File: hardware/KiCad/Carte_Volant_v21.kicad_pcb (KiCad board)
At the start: 4 copper layers, 71.1 x 78.7 mm, 53 parts, among them J1 RJ45_CANBUS_copy, J2 Conn_01x03, J3 Conn_01x40, J7 Conn_01x03, Q2 FDN337N, U1 TSR_1-2450, U2 STM32H103-OlimexBoard, U3 MCP2561-E-SN

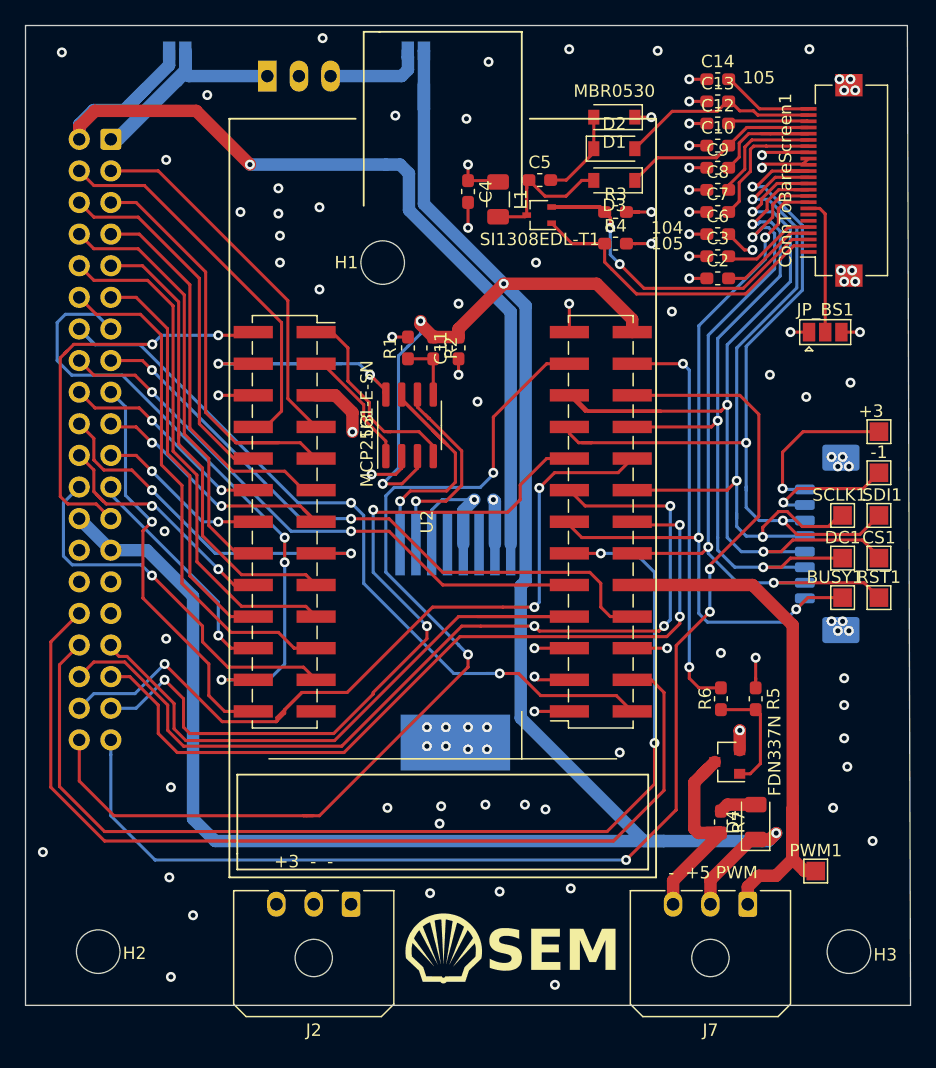
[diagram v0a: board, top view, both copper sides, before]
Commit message: errata correction : RJ45 connector + common volatge source + added 3d models + logo + ...
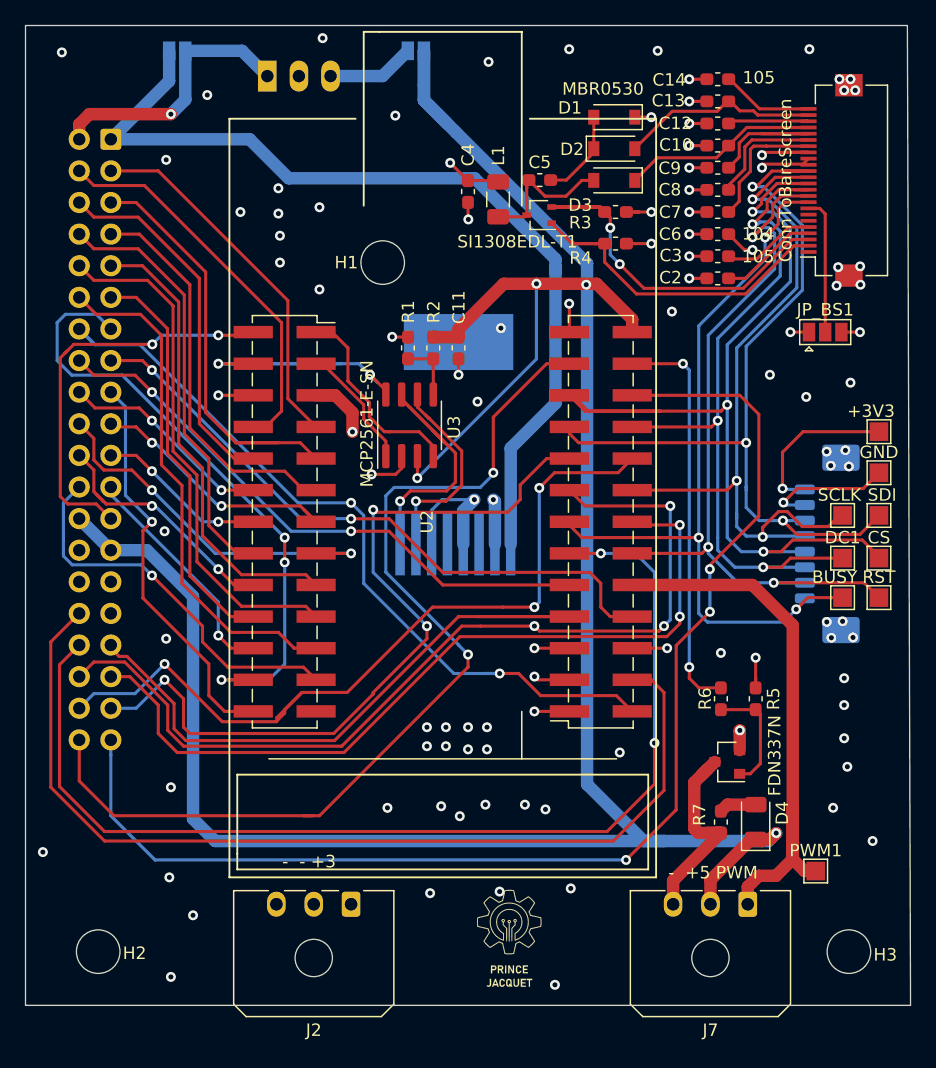
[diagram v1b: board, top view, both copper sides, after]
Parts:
- removed VAL: REF, TIM_Logos_V5:logo_tim07_medium_bottom
- removed VAL: REF, TIM_Logos_V5:logo_shell2_medium_top_silk
- added G***: LOGO, PRINCE LOGO:prince_2_5cm_logo, B.Cu at (147.7, 86.6)
- added G***: LOGO, PRINCE LOGO:prince_1_2cm_logo_nom, F.Cu at (148.6, 102.1)
- C2: value C -> 105
- C5: value C -> 4.7u
- J1: value RJ45_CANBUS_copy -> RJ45_CANBUS
- turned C4 to 90 degrees
- renumbered +3 to +3V3, Alim_12v2 to Alim_12V1, Alim_12v1 to Alim_5V1, BUSY1 to BUSY, CS1 to CS, ConnToBareScreen1 to ConnToBareScreen, -1 to GND, RST1 to RST, SCLK1 to SCLK, SDI1 to SDI
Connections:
- Alim_12V1 pad 1: -POWER_ON-OFF -> +12V
- Alim_12V1 pad 2: POWER_ON-OFF -> POWER_SWITCH
- C4 pad 1: +3V3 -> GND
- C4 pad 2: GND -> +3V3
- ConnToBareScreen pad MP: GND -> (no net)
- ConnToScreenHat1 pad MP: GND -> (no net)
- J1 pad 8: -POWER_ON-OFF -> +12V
- J3 pad 1: POWER_ON-OFF -> +12V
- J3 pad 2: -POWER_ON-OFF -> POWER_SWITCH
- U1 pad 1: POWER_ON-OFF -> POWER_SWITCH
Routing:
- net -POWER_ON-OFF: track 76.7 -> 0.00 mm, vias 1 -> 0
- net +12V: track 0.00 -> 73.6 mm
- net POWER_ON-OFF: track 26.8 -> 0.00 mm
- net POWER_SWITCH: track 0.00 -> 21.9 mm, vias 0 -> 1
- net +5V: track 201.8 -> 207.0 mm
- net GND: track 80.9 -> 85.1 mm, vias 101 -> 83
- net Net-(Alim_5V1-Pad1): track 7.96 -> 7.05 mm
- net +3V3: track 35.9 -> 36.6 mm
- net (no net): vias 0 -> 16
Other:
- board text added: "- - +3"
- board text removed: "+3 - -"
